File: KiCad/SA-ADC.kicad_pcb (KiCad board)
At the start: 2 copper layers, 95.9 x 69.2 mm, 190 parts, among them J1 Conn_01x03, J2 Conn_01x02, J3 Conn_01x08, SW1 SW_Push_SPDT, SW2 SW_Push, U1 74LVC1G04, U10 74LVC1G32, U11 74LVC1G32, U12 74LVC1G32, U13 74LVC1G32, U14 74LVC1G32, U15 74LVC1G32, U16 74LVC1G32, U17 74LVC1G157, U18 74LVC1G157, U19 74LVC1G157, U2 74LVC1G08, U20 74LVC1G157, U21 74LVC1G157, U22 74LVC1G157, U23 74LVC1G157, U24 74LS377, U25 74LVC1G04, U26 74LS377, U27 74LVC1G04, U28 74HC164, U29 74LVC1G175, U3 74LVC1G32, U30 74HC02, U31 74HC02, U34 LM358, U35 74LVC1G125, U37 LM317L_TO92, U38 L7805, U4 74HC245, U44 LM555, U45 74LVC1G125, U47 74LVC1G32, U48 74LVC1G125, U5 74LVC1G32, U6 74LVC1G32, U7 74LVC1G32, U8 74LVC1G32, U9 74LVC1G32

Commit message: PCB v0.2.
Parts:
- removed JP1: Conn_01x03, Connector_PinHeader_2.54mm:PinHeader_1x03_P2.54mm_Vertical
- added SW3: SW_Push_SPDT, Connector_PinHeader_2.54mm:PinHeader_1x03_P2.54mm_Vertical, F.Cu at (110.5, 78.1)
- D1, D19, D2, D20, D21, D22, D23, D24, D25, D26, D27, D28, D29, D3, D30, D31, D32, D33, D34, D35, D36, D37, D38, D39, D4, D40, D41, D42, D43, D5, D6, D7, D8, D9: value LED_Small -> LED
- J1: value Conn_01x03 -> Vin
- J2: value Conn_01x02 -> Power
- J3: value Conn_01x08 -> Out
- U31: value 74HC02 -> 74HC08
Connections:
- R61 pad 2: /SA-Register.sch/Q0 -> /Output/OUT_1
- R62 pad 2: /Output/OUT_1 -> /Output/OUT_2
- R63 pad 2: /Output/OUT_2 -> /Output/OUT_3
- R64 pad 2: /Output/OUT_3 -> /Output/OUT_4
- R65 pad 2: /Output/OUT_4 -> /Output/OUT_5
- R66 pad 2: /Output/OUT_5 -> /Output/OUT_6
- R67 pad 2: /Output/OUT_6 -> /Output/OUT_7
- U31 pad 1: Net-(U31-Pad1) -> Net-(U30-Pad1)
- U31 pad 10: /StateMaschine.sch/C_IN -> Net-(U31-Pad10)
- U31 pad 11: GND -> Net-(U31-Pad11)
- U31 pad 13: Net-(U31-Pad13) -> GND
- U31 pad 2: Net-(U30-Pad1) -> Net-(U30-Pad4)
- U31 pad 3: Net-(U30-Pad4) -> Net-(U31-Pad3)
- U31 pad 4: Net-(U31-Pad4) -> Net-(U30-Pad10)
- U31 pad 5: Net-(U30-Pad10) -> Net-(U30-Pad13)
- U31 pad 6: Net-(U30-Pad13) -> Net-(U31-Pad10)
- U31 pad 8: Net-(U31-Pad1) -> /StateMaschine.sch/C_IN
- U31 pad 9: Net-(U31-Pad4) -> Net-(U31-Pad3)
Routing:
- net /StateMaschine.sch/C_IN: track 17.3 -> 58.4 mm, vias 0 -> 4
- net /Output/OUT_7: track 48.9 -> 80.4 mm, vias 4 -> 5
- net Net-(U30-Pad1): track 17.5 -> 31.0 mm
- net Net-(U31-Pad1): track 12.4 -> 0.00 mm, vias 2 -> 0
- net Net-(U31-Pad3): track 0.00 -> 8.76 mm, vias 0 -> 2
- net /Output/OUT_3: track 60.4 -> 68.2 mm
- net /Output/OUT_4: track 116.6 -> 124.2 mm
- net /Output/OUT_6: track 96.7 -> 103.9 mm, vias 9 -> 8
- net Net-(U31-Pad10): track 0.00 -> 6.45 mm
- net Net-(U31-Pad4): track 6.03 -> 0.00 mm
- net GND: track 882.2 -> 887.6 mm
- net Net-(U30-Pad13): track 13.3 -> 18.1 mm
- net /Output/OUT_5: track 88.5 -> 84.3 mm
- net +5V: track 688.0 -> 685.1 mm
- net Net-(U30-Pad4): track 24.7 -> 26.2 mm, vias 3 -> 2
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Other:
- board text added: "v0.2"
- board text removed: "v0.1"

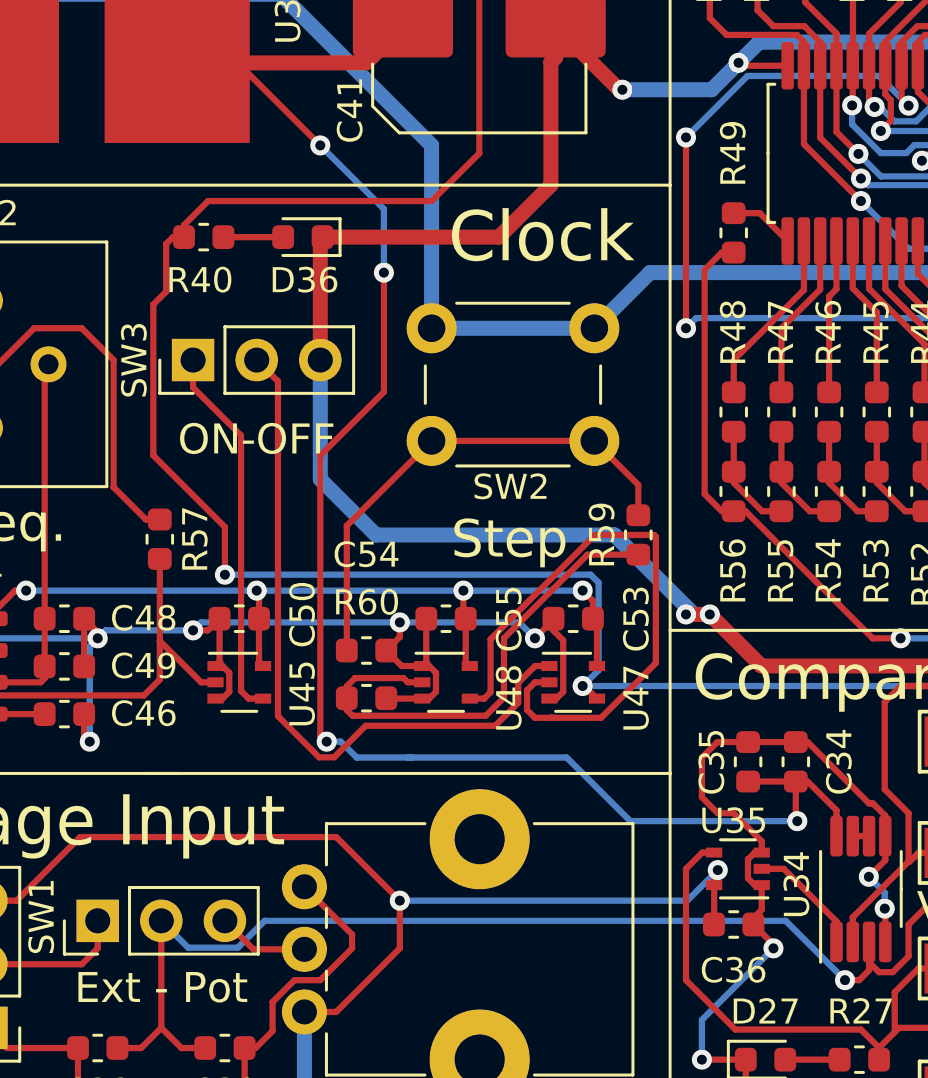
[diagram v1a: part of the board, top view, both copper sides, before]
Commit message: v0.3 Changed to Schmitt-Trigger ICs Added pull-down resistor to Clock Enable
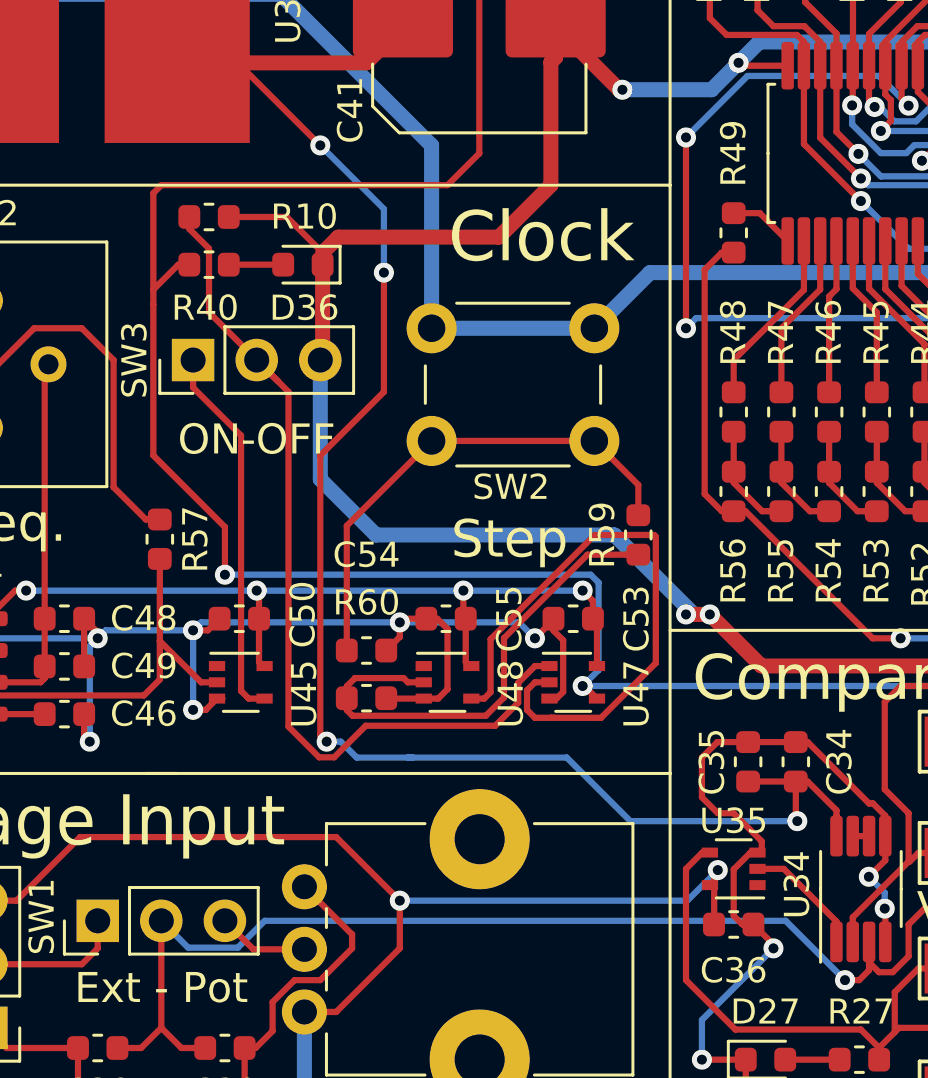
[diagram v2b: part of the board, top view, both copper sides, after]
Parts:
- added R10: 10K, Resistor_SMD:R_0603_1608Metric, F.Cu at (111.1, 72.4)
- C54: value TBD -> 0u1
- R1, R19, R2, R20, R21, R22, R23, R24, R25, R26, R27, R28, R29, R3, R30, R31, R32, R33, R34, R35, R4, R40, R5, R6, R61, R62, R63, R64, R65, R66, R67, R7, R8, R9: value rled -> 39K
- R41, R42, R43, R44, R45, R46, R47, R48, R49: value 20K -> 20K 0.1%
- R50, R51, R52, R53, R54, R55, R56: value 10K -> 10K 0.1%
- R59, R60: value TBD -> 10K
- U1, U25, U27: value 74LVC1G04 -> SN74LVC1G04DCK
- U10, U11, U12, U13, U14, U15, U16, U3, U47, U5, U6, U7, U8, U9: value 74LVC1G32 -> SN74LVC1G32DCK
- U17, U18, U19, U20, U21, U22, U23: value 74LVC1G157 -> 74LVC1G157GW
- U2: value 74LVC1G08 -> SN74LVC1G08DCK
- U24, U26: value 74LS377 -> SN74HC377DW
- U28: value 74HC164 -> 74HC161D
- U29: value 74LVC1G175 -> SN74LVC1G175DCK
- U30: value 74HC02 -> SN74HC02D
- U31: value 74HC08 -> SN74HC08D
- U34: value LM358 -> LM358ST
- U35, U45, U48: value 74LVC1G125 -> 74LVC1G17DCK
- U37: value LM317L_TO92 -> LM317
- U38: value L7805 -> L7805CDT
- U4: value 74HC245 -> SN74HC245DBR
- U44: value LM555 -> NE555DR
- moved R40 1.12 mm to (111.1, 74.3)
- moved D36 1.10 mm to (114.9, 74.3)
- moved U35 0.17 mm to (132.1, 98.4)
- moved U48 0.06 mm to (120.7, 91.0)
- moved U45 0.06 mm to (112.4, 91.0)
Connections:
- RV2 pad 3: Net-(RV2-Pad3) -> (no net)
- U24 pad 19: Net-(U24-Pad19) -> (no net)
- U31 pad 11: Net-(U31-Pad11) -> (no net)
- U35 pad 1: GND -> (no net)
- U44 pad 7: Net-(U44-Pad7) -> (no net)
- U45 pad 1: GND -> (no net)
- U48 pad 1: GND -> (no net)
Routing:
- net Net-(R10-Pad2): track 28.1 -> 36.1 mm
- net GND: track 887.6 -> 893.1 mm, vias 44 -> 45
- net /Clock/CLK: track 195.4 -> 198.5 mm
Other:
- board text added: "v0.3"
- board text removed: "v0.2"
